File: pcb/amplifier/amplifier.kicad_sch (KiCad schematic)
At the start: 17 parts, among them IC1 PA441DF, J1 Screw_Terminal_01x02, J2 Screw_Terminal_01x02, J3 Screw_Terminal_01x02, J4 Screw_Terminal_01x02

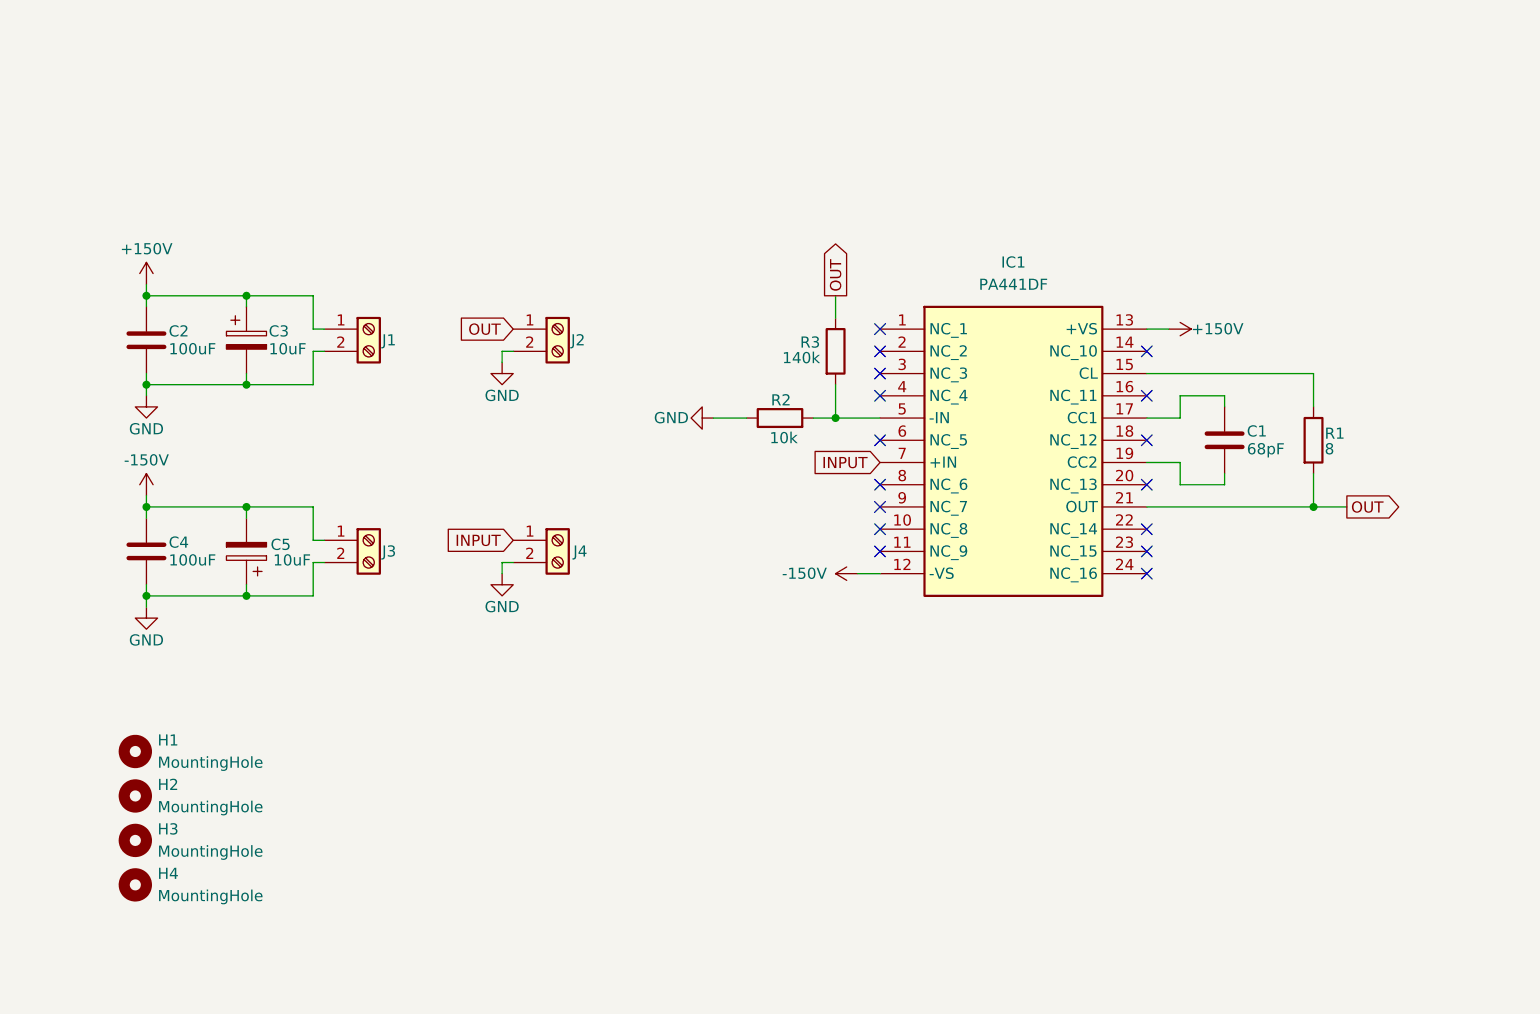
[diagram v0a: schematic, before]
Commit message: change to inverting opamp configuration
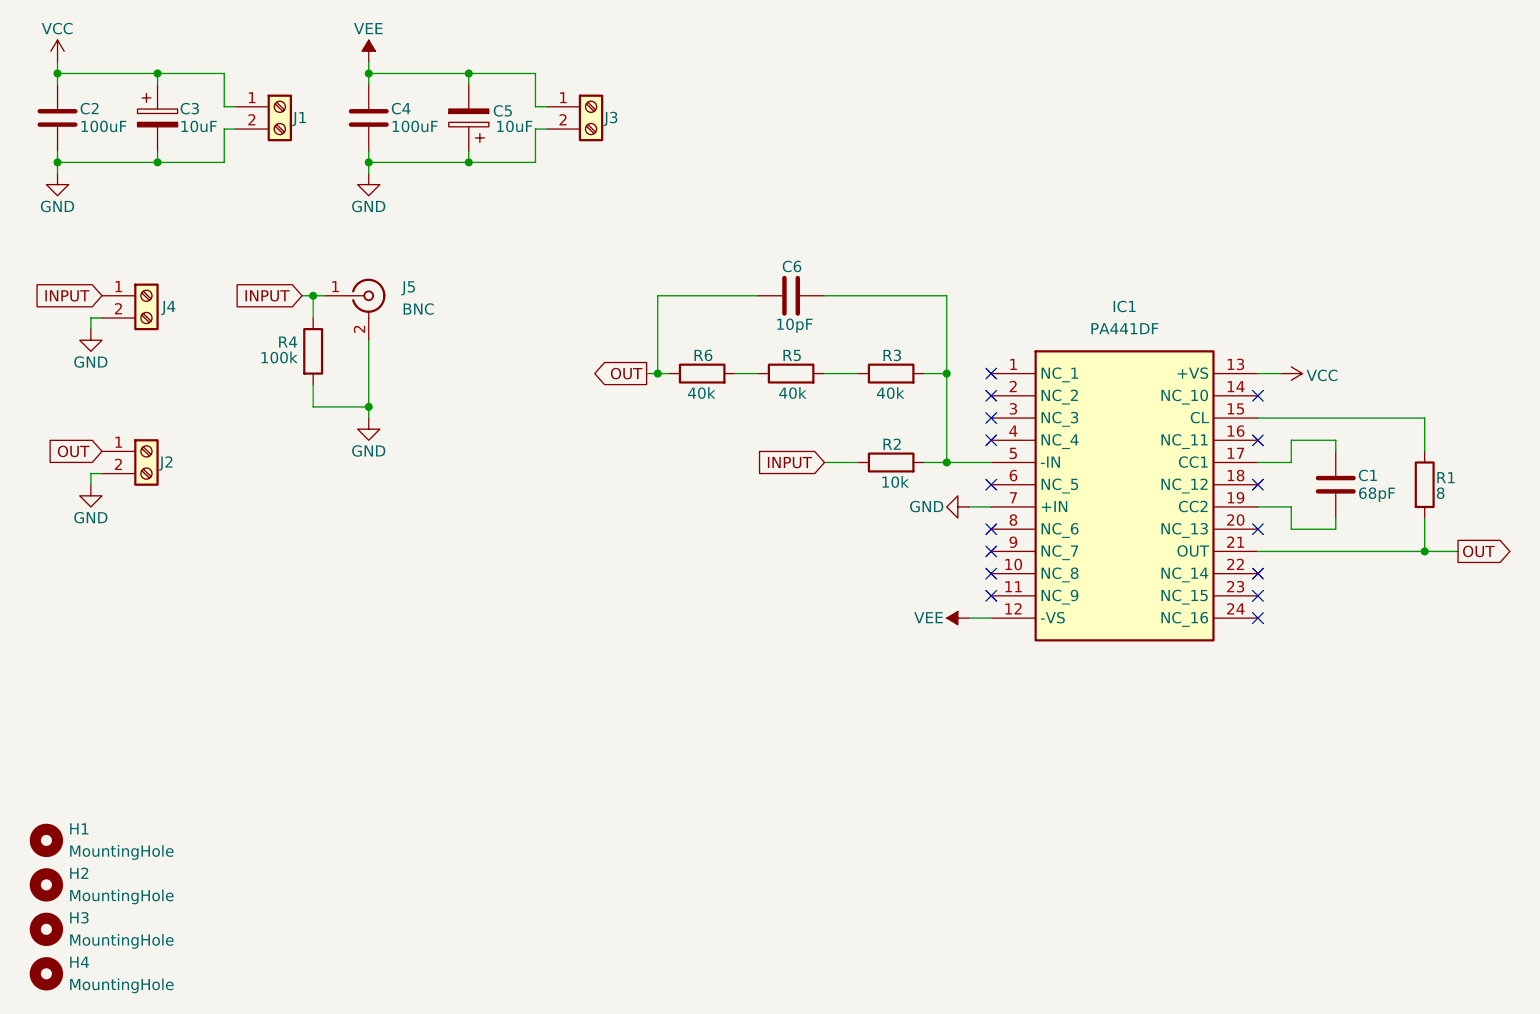
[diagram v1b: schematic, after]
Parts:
- added C6: 10pF, symbol Device:C
- added J5: BNC, symbol Connector:Conn_Coaxial
- added R4: 100k, symbol Device:R
- added R5, R6: 40k, symbol Device:R
- R3: value 140k -> 40k
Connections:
- net GND: now also IC1.7 (+IN), J5.2 (Ext), R4.2; no longer R2.1
- net INPUT: now also R2.1, J5.1 (In), R4.1; no longer IC1.7 (+IN)
- net OUT: now also C6.1, R6.1; no longer R3.1
- net at IC1.5 (-IN), R2.2, R3.2: now also C6.2
- net +150V renamed VCC
- net -150V renamed VEE
- new net: R3.1, R5.2
- new net: R5.1, R6.2
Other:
- moved on the sheet: C1, C2, C3, C4, C5, H1, H2, H3, H4, IC1, J1, J2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
